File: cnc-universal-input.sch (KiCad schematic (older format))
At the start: 123 parts, among them J1 3PT, J10 2PT, J11 8PT, J12 USB_B_Mini, J13 2PT, J14 2PT, J2 3PT, J3 3PT, J4 3PT, J5 3PT, J6 3PT, J7 3PT, J8 3PT, J9 AVR-ISP-6, Q1 2N7002, Q11 2N7002, Q12 2N7002, Q13 2N7002, SW1 RESET, SW2 BTN, U1 ATmega328PB-AU, U10 SFH617A-4, U11 SFH617A-4, U12 SFH617A-4, U13 SFH617A-4, U14 SFH617A-4, U15 SFH617A-4, U16 SFH617A-4, U18 CH340G, U19 TS2596S, U2 74HC595, U3 74HC595, U4 74HC595, U5 4051, U6 TS2596S, U8 LM7321, U9 SFH617A-4, Y1 16MHz, Y2 12MHz

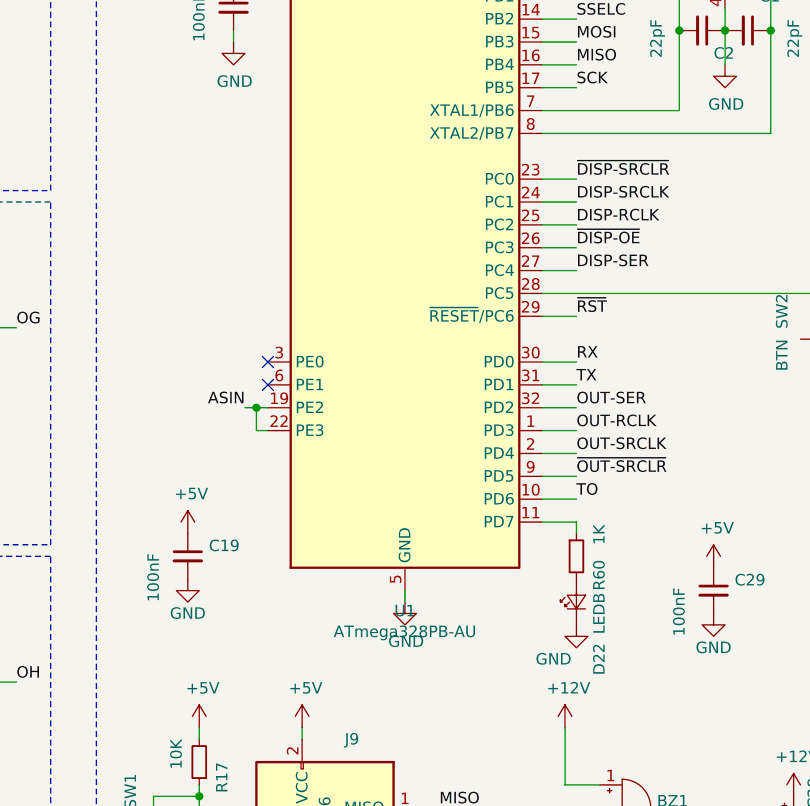
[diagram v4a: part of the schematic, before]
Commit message: Fixed missing and broken step files
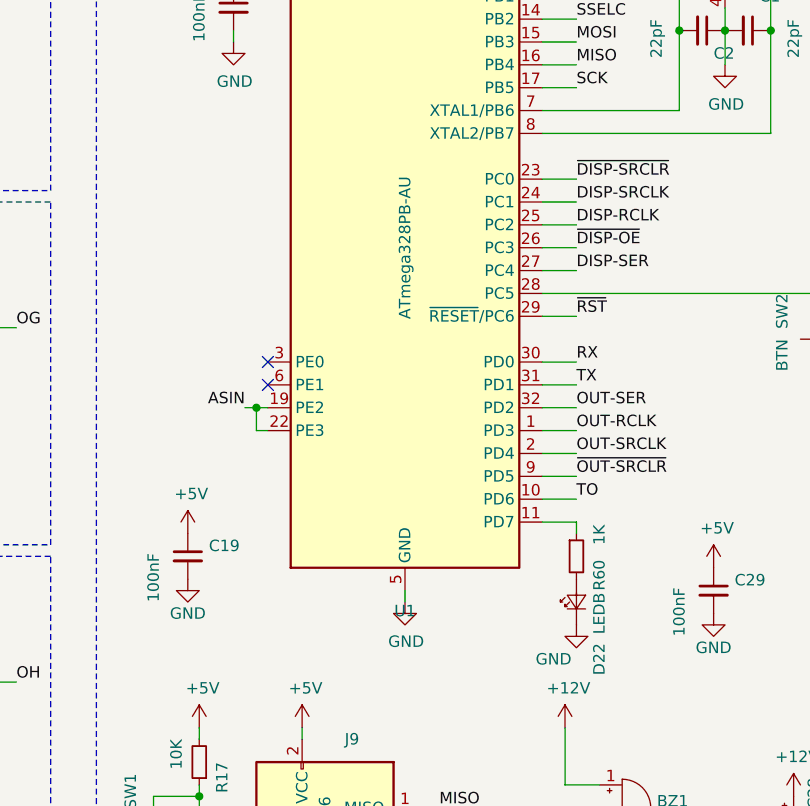
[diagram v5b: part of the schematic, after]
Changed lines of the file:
@@
 encoding utf-8
 Sheet 1 1
-Title ""
-Date ""
-Rev ""
-Comp ""
+Title "UCNC"
+Date "2021-08-13"
+Rev "1.5"
+Comp "IvyBit"
 Comment1 ""
 Comment2 ""
@@
 P 10550 6200
 F 0 "U1" H 10550 4611 50  0000 C CNN
-F 1 "ATmega328PB-AU" H 10550 4520 50  0000 C CNN
+F 1 "ATmega328PB-AU" V 10550 6200 50  0000 C CNN
 F 2 "Package_QFP:TQFP-32_7x7mm_P0.8mm" H 10550 6200 50  0001 C CIN
 F 3 "http://ww1.microchip.com/downloads/en/DeviceDoc/40001906C.pdf" H 10550 6200 50  0001 C CNN

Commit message: Cap be gone
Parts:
- removed C25: 10uF, Capacitor_SMD:CP_Elec_4x5.4, symbol Device:CP_Small
- removed C26: 100nF, Capacitor_SMD:C_0805_2012Metric, symbol Device:C_Small
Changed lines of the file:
@@
-	1    0    0    -1
-$EndComp
-$Comp
-L power:+5VD #PWR0147
-U 1 1 606CE08E
-P 15500 850
-F 0 "#PWR0147" H 15500 700 50  0001 C CNN
-F 1 "+5VD" H 15515 1023 50  0000 C CNN
-F 2 "" H 15500 850 50  0001 C CNN
-F 3 "" H 15500 850 50  0001 C CNN
-	1    15500 850
-	1    0    0    -1
-$EndComp
-$Comp
-L power:+5VD #PWR0146
-U 1 1 606CDC8B
-P 15300 850
-F 0 "#PWR0146" H 15300 700 50  0001 C CNN
-F 1 "+5VD" H 15315 1023 50  0000 C CNN
-F 2 "" H 15300 850 50  0001 C CNN
-F 3 "" H 15300 850 50  0001 C CNN
-	1    15300 850
-	1    0    0    -1
-$EndComp
-$Comp
-L power:GND #PWR0145
-U 1 1 60664040
-P 15300 1050
-F 0 "#PWR0145" H 15300 800 50  0001 C CNN
-F 1 "GND" H 15300 900 50  0000 C CNN
-F 2 "" H 15300 1050 50  0001 C CNN
-F 3 "" H 15300 1050 50  0001 C CNN
-	1    15300 1050
-	1    0    0    -1
-$EndComp
-$Comp
-L Device:CP_Small C25
-U 1 1 6066403A
-P 15300 950
-F 0 "C25" V 15388 996 50  0000 L CNN
-F 1 "10uF" V 15150 800 50  0000 L CNN
-F 2 "Capacitor_SMD:CP_Elec_4x5.4" H 15300 950 50  0001 C CNN
-F 3 "~" H 15300 950 50  0001 C CNN
-	1    15300 950
-	1    0    0    -1
-$EndComp
-$Comp
-L power:GND #PWR0144
-U 1 1 6066402E
-P 15500 1050
-F 0 "#PWR0144" H 15500 800 50  0001 C CNN
-F 1 "GND" H 15500 900 50  0000 C CNN
-F 2 "" H 15500 1050 50  0001 C CNN
-F 3 "" H 15500 1050 50  0001 C CNN
-	1    15500 1050
-	1    0    0    -1
-$EndComp
-$Comp
-L Device:C_Small C26
-U 1 1 60664028
-P 15500 950
-F 0 "C26" H 15600 850 50  0000 L CNN
-F 1 "100nF" V 15700 900 50  0000 L CNN
-F 2 "Capacitor_SMD:C_0805_2012Metric" H 15500 950 50  0001 C CNN
-F 3 "~" H 15500 950 50  0001 C CNN
-	1    15500 950
 	1    0    0    -1
 $EndComp

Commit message: assemble all the things!
JLCPCB please make my life easier!!
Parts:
- removed C10, C5: 10uF, Capacitor_SMD:CP_Elec_4x5.4, symbol Device:CP_Small
- removed C14, C8: 100nF, Capacitor_SMD:C_0805_2012Metric, symbol Device:C_Small
- removed C15, C24: 10nF, Capacitor_SMD:C_0805_2012Metric, symbol Device:C_Small
- removed J11: 8PT, TerminalBlock_RND:TerminalBlock_RND_205-00007_1x08_P5.00mm_Horizontal, symbol Connector:Screw_Terminal_01x08
- removed R72: 4.7K, Resistor_SMD:R_0805_2012Metric, symbol Device:R_Small
- removed R73: 1.5K, Resistor_SMD:R_0805_2012Metric, symbol Device:R_Small
- removed R74: 9.1K, Resistor_SMD:R_0805_2012Metric, symbol Device:R_Small
- removed R75: 1K, Resistor_SMD:R_0805_2012Metric, symbol Device:R_Small
- removed RN11, RN12: 470P4, Resistor_SMD:R_Array_Convex_4x0603, symbol Device:R_Pack04
- removed Y2: 12MHz, Crystal:Crystal_HC49-4H_Vertical, symbol Device:Crystal_Small
- added C10, C5: 100nF, Capacitor_SMD:C_0805_2012Metric, symbol Device:C_Small
- added C14, C15, C24, C25, C26, C8: 10uF, Capacitor_SMD:C_1206_3216Metric, symbol Device:CP_Small
- added D27: LEDO, Diode_SMD:D_0805_2012Metric, symbol Device:LED_Small
- added J15, J16, J17, J18: 2PT, TerminalBlock_RND:TerminalBlock_RND_205-00001_1x02_P5.00mm_Horizontal, symbol Connector:Screw_Terminal_01x02
- added Q2, Q3, Q4, Q5, Q6, Q7, Q8, Q9: 2N7002, Package_TO_SOT_SMD:SOT-23, symbol Transistor_FET:2N7002
- added R1, R2, R3, R4, R5, R6, R7, R8: 220, Resistor_SMD:R_0805_2012Metric, symbol Device:R_Small
- added R9: 1K, Resistor_SMD:R_0805_2012Metric, symbol Device:R_Small
- added TP1: GND, TestPoint:TestPoint_Pad_D1.5mm, symbol Connector:TestPoint_Probe
- added TP2: +24V, TestPoint:TestPoint_Pad_D1.5mm, symbol Connector:TestPoint_Probe
- added TP3: +5V, TestPoint:TestPoint_Pad_D1.5mm, symbol Connector:TestPoint_Probe
- added TP4: +12V, TestPoint:TestPoint_Pad_D1.5mm, symbol Connector:TestPoint_Probe
- added U7: ADuM1201AR, Package_SO:SOIC-8_3.9x4.9mm_P1.27mm, symbol Isolator:ADuM1201AR
- added Y2: 12MHz, Crystal:Crystal_SMD_3225-4Pin_3.2x2.5mm, symbol Device:Crystal_GND24
- BZ1: footprint Buzzer_Beeper:MagneticBuzzer_ProSignal_ABT-410-RC -> Buzzer_Beeper:Buzzer_15x7.5RM7.6; LCSC (none) -> C128017
- C1, C2: LCSC (none) -> C1804
- C11, C12: value 30pF -> 22pF; LCSC (none) -> C1804
- C13, C16, C17, C18, C19, C20, C21, C23, C29, C4, C9: LCSC (none) -> C49678
- C22, C27, C28: footprint Capacitor_SMD:CP_Elec_4x5.4 -> Capacitor_SMD:C_1206_3216Metric; LCSC (none) -> C13585
- C3: value 150uF -> 470uF; footprint Capacitor_SMD:CP_Elec_6.3x7.7 -> Capacitor_SMD:CP_Elec_10x10; LCSC (none) -> C3350
- C6, C7: LCSC (none) -> C3342
- D1, D19, D2, D3, D4, D5, D6, D7, D8: LCSC (none) -> C205444
- D10, D11, D12, D13, D14, D15, D16, D18, D22, D9: LCSC (none) -> C205441
- D17: LCSC (none) -> C294621
- D20, D21: value B240F -> SS36-E3/57T; LCSC (none) -> C35722
- D23, D24, D25, D26: LCSC (none) -> C556167
- J1, J2, J3, J4, J5, J6, J7, J8: LCSC (none) -> C8270
- J10, J13, J14: LCSC (none) -> C8404
- J12: LCSC (none) -> C1121886
- J9: LCSC (none) -> C192301
- L1, L2: footprint Inductor_SMD:L_6.3x6.3_H3 -> Inductor_SMD:L_12x12mm_H8mm; LCSC (none) -> C169377
- Q1, Q11, Q12, Q13: LCSC (none) -> C8545
- R17, R34, R68, R69, R70, R71: LCSC (none) -> C17724
- R35: LCSC (none) -> C17772
- R60: LCSC (none) -> C17513
- R66, R67: LCSC (none) -> C17604
- RN1, RN2: value 10KP4 -> 4.7KP4; LCSC (none) -> C66697
- RN10, RN7, RN8, RN9: LCSC (none) -> C66697
- RN3, RN4: value 470P4 -> 330P4; LCSC (none) -> C12018
- RN5, RN6: value 470P4 -> 620P4; LCSC (none) -> C12034
- SW1, SW2: footprint Button_Switch_SMD:SW_SPST_B3S-1000 -> Button_Switch_SMD:SW_SPST_TL3342; LCSC (none) -> C318884
- U1: LCSC (none) -> C132230
- U10, U11, U12, U13, U14, U15, U16, U9: value SFH617A-4 -> EL357NC; footprint Package_DIP:DIP-4_W7.62mm -> IvyBit-footprints:SOP-4_4.1x4.4x2.54P; LCSC (none) -> C29981
- U18: LCSC (none) -> C14267
- U19: value TS2596S -> XL1509-5E1; footprint Package_SO:SOP-8_3.9x4.9mm_P1.27mm -> Package_SO:SOIC-8_3.9x4.9mm_P1.27mm; LCSC (none) -> C61063
- U2, U3, U4: LCSC (none) -> C5947
- U5: LCSC (none) -> C21379
- U6: value TS2596S -> XL1509-12E1; footprint Package_SO:SOP-8_3.9x4.9mm_P1.27mm -> Package_SO:SOIC-8_3.9x4.9mm_P1.27mm; LCSC (none) -> C62594
- U8: value LM7321 -> SGMOP07CXS8G/TR; LCSC (none) -> C89712
- Y1: footprint Crystal:Crystal_SMD_EuroQuartz_MJ-4Pin_5.0x3.2mm -> Crystal:Crystal_SMD_3225-4Pin_3.2x2.5mm; LCSC (none) -> C13738
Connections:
- net +12V: now also U6.3 (FB), C14.1, C24.1, C26.1, TP4.1
- net +24V: now also TP2.1
- net +5V: now also U19.3 (FB), C10.2, C15.1, C8.1, R1.1, R2.1, R3.1, R4.1, R5.1, R6.1, R7.1, R8.1, TP3.1, U7.8 (VDD2); no longer C21.1, R66.1, R67.1, U18.16 (VCC)
- net BA: now also J15.1 (Pin_1)
- net BB: now also J15.2 (Pin_2)
- net BC: now also J16.1 (Pin_1)
- net BD: now also J16.2 (Pin_2)
- net BE: now also J17.1 (Pin_1)
- net BF: now also J17.2 (Pin_2)
- net BG: now also J18.1 (Pin_1)
- net BH: now also J18.2 (Pin_2)
- net GND: now also C10.1, C14.2, C15.2, C24.2, C26.2, C8.2, Q2.2 (S), Q3.2 (S), Q4.2 (S), Q5.2 (S), Q6.2 (S), Q7.2 (S), Q8.2 (S), Q9.2 (S), TP1.1, U7.5 (GND2); no longer C11.1, C12.1, C13.2, C21.2, J12.5 (GND), U10.2, U11.2, U12.2, U13.2, U14.2, U15.2, U16.2, U18.1 (GND), U9.2
- net OUT-A: now also Q2.1 (G)
- net OUT-B: now also Q3.1 (G)
- net OUT-C: now also Q4.1 (G)
- net OUT-D: now also Q5.1 (G)
- net OUT-E: now also Q7.1 (G)
- net OUT-F: now also Q6.1 (G)
- net OUT-G: now also Q8.1 (G)
- net OUT-H: now also Q9.1 (G)
- net at U18.7 (XI): now also C12.1, Y2.3; no longer C11.2
- net at U18.8 (XO): now also C11.2, Y2.1; no longer C12.2
- net VBUS: now reaches J12.1 (VBUS)
- net VBUS: now also C21.1, R66.1, R67.1, U18.16 (VCC), C25.1, C5.2, R9.1, U7.1 (VDD1)
- net POA: no longer names the net of U9.1
- net POA: now also R1.2
- net POB: no longer names the net of U10.1
- net POB: now also R2.2
- net POC: no longer names the net of U11.1
- net POC: now also R3.2
- net POD: no longer names the net of U12.1
- net POD: now also R4.2
- net POE: no longer names the net of U13.1
- net POE: now also R6.2
- net POF: no longer names the net of U14.1
- net POF: now also R5.2
- net POG: no longer names the net of U15.1
- net POG: now also R7.2
- net POH: no longer names the net of U16.1
- net POH: now also R8.2
- net RX renamed RX1
- net RX1: now also U7.3 (VIB); no longer U1.30 (PD0)
- net TX renamed TX1
- net TX1: now also U7.2 (VOA); no longer U1.31 (PD1)
- new net: Q2.3 (D), U9.2
- new net: Q7.3 (D), U13.2
- new net: Q3.3 (D), U10.2
- new net: Q4.3 (D), U11.2
- new net: Q5.3 (D), U12.2
- new net: Q6.3 (D), U14.2
- new net: Q8.3 (D), U15.2
- new net: Q9.3 (D), U16.2
- new net: D27.2 (A), R9.2
- new net GND_USB: C11.1, C12.2, C13.2, C21.2, C25.2, C5.1, D27.1 (K), J12.5 (GND), U18.1 (GND), U7.4 (GND1), Y2.2, Y2.4
- new net RX2: U1.30 (PD0), U7.6 (VOB)
- new net TX2: U1.31 (PD1), U7.7 (VIA)
- no-connect marks 14 -> 13
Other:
- moved on the sheet: C21, C9, J10, J12, J14, U10, U13, U9

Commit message: Nothing! Absolutely Nothing!
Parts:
- BZ1: symbol Device:Buzzer -> cnc-universal-input-rescue:Buzzer-Device
- C1, C10, C11, C12, C13, C16, C17, C18, C19, C2, C20, C21, C23, C29, C4, C5, C9: symbol Device:C_Small -> cnc-universal-input-rescue:C_Small-Device
- C14, C15, C22, C24, C25, C26, C27, C28, C3, C6, C7, C8: symbol Device:CP_Small -> cnc-universal-input-rescue:CP_Small-Device
- D1, D10, D11, D12, D13, D14, D15, D16, D18, D19, D2, D22, D27, D3, D4, D5, D6, D7, D8, D9: symbol Device:LED_Small -> cnc-universal-input-rescue:LED_Small-Device
- D17: symbol Diode:BZX84Cxx -> cnc-universal-input-rescue:BZX84Cxx-Diode
- D20, D21: symbol Device:D_Schottky_Small -> cnc-universal-input-rescue:D_Schottky_Small-Device
- D23, D24, D25, D26: symbol Diode:BAT54A -> cnc-universal-input-rescue:BAT54A-Diode
- J1, J2, J3, J4, J5, J6, J7, J8: symbol Connector:Screw_Terminal_01x03 -> cnc-universal-input-rescue:Screw_Terminal_01x03-Connector
- J10, J13, J14, J15, J16, J17, J18: symbol Connector:Screw_Terminal_01x02 -> cnc-universal-input-rescue:Screw_Terminal_01x02-Connector
- J9: symbol Connector:AVR-ISP-6 -> cnc-universal-input-rescue:AVR-ISP-6-Connector
- L1, L2: symbol Device:L_Small -> cnc-universal-input-rescue:L_Small-Device
- Q1, Q11, Q12, Q13, Q2, Q3, Q4, Q5, Q6, Q7, Q8, Q9: symbol Transistor_FET:2N7002 -> cnc-universal-input-rescue:2N7002-Transistor_FET
- R1, R17, R2, R3, R34, R35, R4, R5, R6, R60, R66, R67, R68, R69, R7, R70, R71, R8, R9: symbol Device:R_Small -> cnc-universal-input-rescue:R_Small-Device
- RN1, RN10, RN2, RN3, RN4, RN5, RN6, RN7, RN8, RN9: symbol Device:R_Pack04 -> cnc-universal-input-rescue:R_Pack04-Device
- SW1, SW2: symbol Switch:SW_Push -> cnc-universal-input-rescue:SW_Push-Switch
- TP1, TP2, TP3, TP4: symbol Connector:TestPoint_Probe -> cnc-universal-input-rescue:TestPoint_Probe-Connector
- U1: symbol MCU_Microchip_ATmega:ATmega328PB-AU -> cnc-universal-input-rescue:ATmega328PB-AU-MCU_Microchip_ATmega
- U10, U11, U12, U13, U14, U15, U16, U9: symbol Isolator:SFH617A-4 -> cnc-universal-input-rescue:SFH617A-4-Isolator
- U18: symbol Interface_USB:CH340G -> cnc-universal-input-rescue:CH340G-Interface_USB
- U2, U3, U4: symbol 74xx:74HC595 -> cnc-universal-input-rescue:74HC595-74xx
- U5: symbol 4xxx:4051 -> cnc-universal-input-rescue:4051-4xxx
- U7: symbol Isolator:ADuM1201AR -> cnc-universal-input-rescue:ADuM1201AR-Isolator
- U8: symbol Amplifier_Operational:AD8001AR -> cnc-universal-input-rescue:AD8001AR-Amplifier_Operational
- Y1, Y2: symbol Device:Crystal_GND24 -> cnc-universal-input-rescue:Crystal_GND24-Device
